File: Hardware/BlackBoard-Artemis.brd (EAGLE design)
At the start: 68.6 x 53.3 mm, 130 parts, among them IC3 LM1117, J2 CORTEX_DEBUG, J3 POWER_JACKTOE, J5 USB-C, Q1 1.1A/60V/600mΩ, U3 AP2112-3.3V, U4 ARTEMIS_MODULESMD, U5 CH340C, Y1 32.768kHz

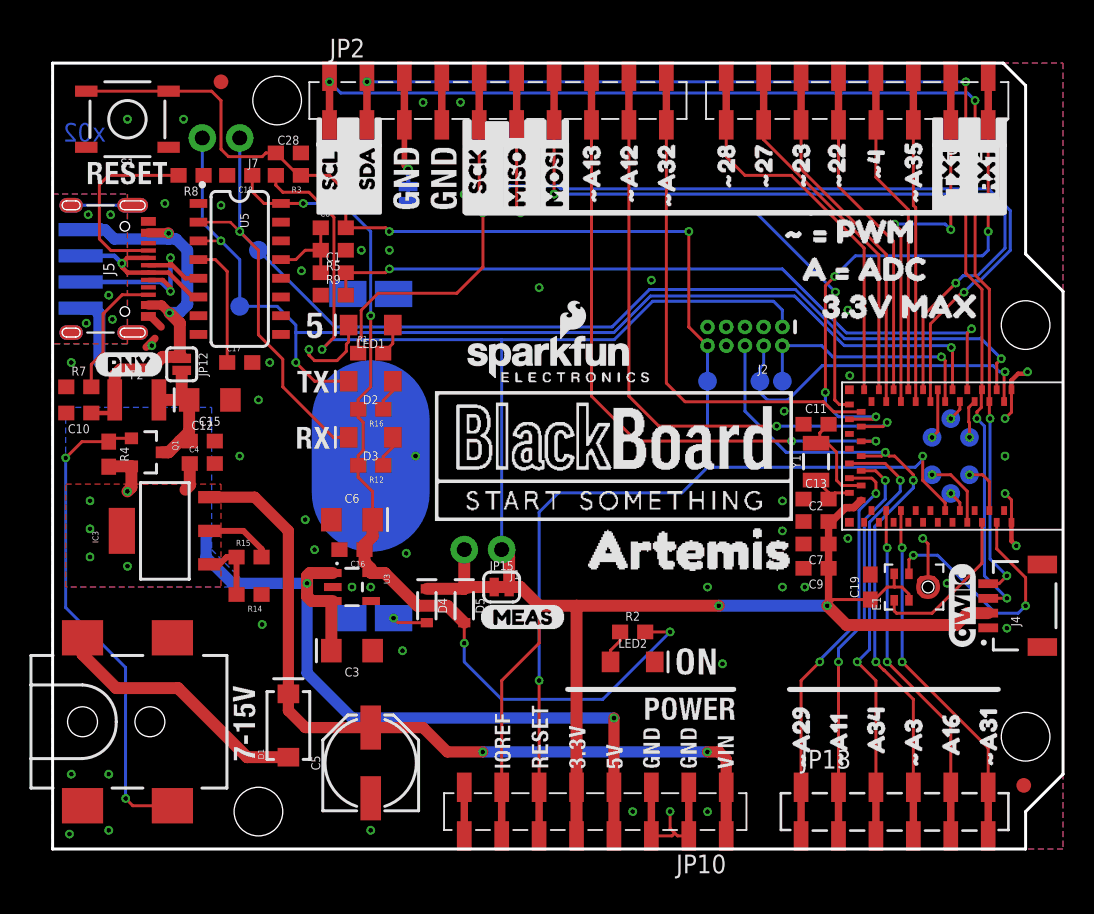
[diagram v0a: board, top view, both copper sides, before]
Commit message: Adding production panel
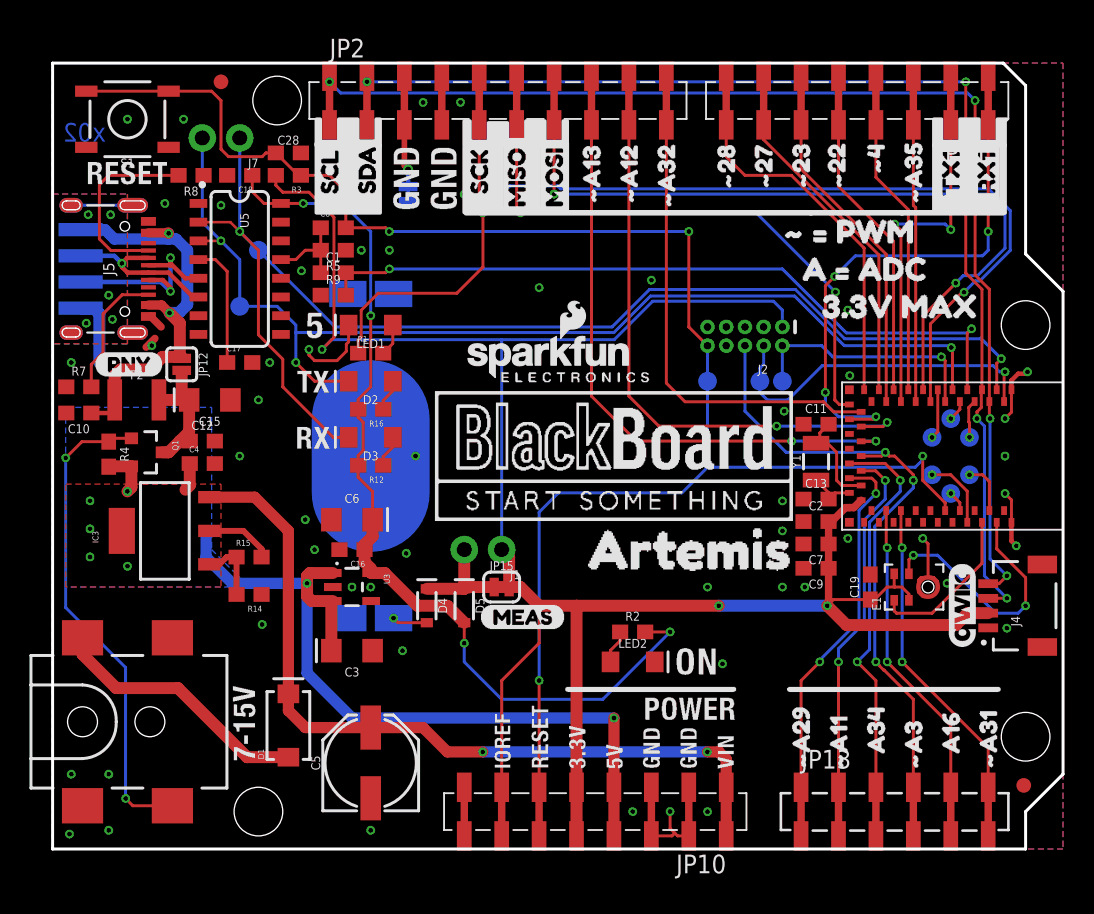
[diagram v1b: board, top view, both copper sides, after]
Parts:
- removed U$57: (no value), buzzard_labels (10):SCL3
- removed U$58: (no value), buzzard_labels (10):SDA4
- added U$18: (no value), buzzard_labels (6):SCL1
- added U$22: (no value), buzzard_labels (6):SDA0
- moved U$19 0.38 mm to (55.9, 44.8)
- moved U$17 0.13 mm to (61.0, 5.46)
- moved U$28 0.13 mm to (58.4, 4.45)
- moved U$29 0.13 mm to (53.3, 4.45)
- moved U$31 0.13 mm to (63.5, 4.45)
- moved U$50 0.13 mm to (29.0, 43.4)

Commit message: Fixing PWM on pin 7
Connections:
- net D7/MOSI renamed ~D7/MOSI
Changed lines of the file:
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@@
 <grid distance="0.05" unitdist="inch" unit="inch" style="lines" multiple="1" display="yes" altdistance="0.005" altunitdist="inch" altunit="inch"/>
 <layers>
-<layer number="1" name="Top" color="4" fill="1" visible="no" active="yes"/>
-<layer number="16" name="Bottom" color="1" fill="1" visible="no" active="yes"/>
+<layer number="1" name="Top" color="4" fill="1" visible="yes" active="yes"/>
+<layer number="16" name="Bottom" color="1" fill="1" visible="yes" active="yes"/>
 <layer number="17" name="Pads" color="2" fill="1" visible="yes" active="yes"/>
-<layer number="18" name="Vias" color="2" fill="1" visible="no" active="yes"/>
-<layer number="19" name="Unrouted" color="6" fill="1" visible="no" active="yes"/>
+<layer number="18" name="Vias" color="2" fill="1" visible="yes" active="yes"/>
+<layer number="19" name="Unrouted" color="6" fill="1" visible="yes" active="yes"/>
 <layer number="20" name="Dimension" color="24" fill="1" visible="yes" active="yes"/>
 <layer number="21" name="tPlace" color="16" fill="1" visible="yes" active="yes"/>
-<layer number="22" name="bPlace" color="14" fill="1" visible="no" active="yes"/>
+<layer number="22" name="bPlace" color="14" fill="1" visible="yes" active="yes"/>
 <layer number="23" name="tOrigins" color="15" fill="1" visible="yes" active="yes"/>
-<layer number="24" name="bOrigins" color="15" fill="1" visible="no" active="yes"/>
+<layer number="24" name="bOrigins" color="15" fill="1" visible="yes" active="yes"/>
 <layer number="25" name="tNames" color="7" fill="1" visible="no" active="yes"/>
 <layer number="26" name="bNames" color="7" fill="1" visible="no" active="yes"/>
-<layer number="27" name="tValues" color="7" fill="1" visible="yes" active="yes"/>
+<layer number="27" name="tValues" color="7" fill="1" visible="no" active="yes"/>
 <layer number="28" name="bValues" color="7" fill="1" visible="no" active="yes"/>
 <layer number="29" name="tStop" color="2" fill="3" visible="no" active="yes"/>
 <layer number="30" name="bStop" color="5" fill="6" visible="no" active="yes"/>
-<layer number="31" name="tCream" color="7" fill="4" visible="yes" active="yes"/>
+<layer number="31" name="tCream" color="7" fill="4" visible="no" active="yes"/>
 <layer number="32" name="bCream" color="7" fill="5" visible="no" active="yes"/>
 <layer number="33" name="tFinish" color="6" fill="3" visible="no" active="yes"/>
@@
 <wire x1="61.079" y1="33.9551" x2="61.079" y2="31.17" width="0.2032" layer="1"/>
 </signal>
-<signal name="D7/MOSI">
+<signal name="~D7/MOSI">
 <contactref element="JP2" pad="7B"/>
 <contactref element="JP2" pad="7A"/>

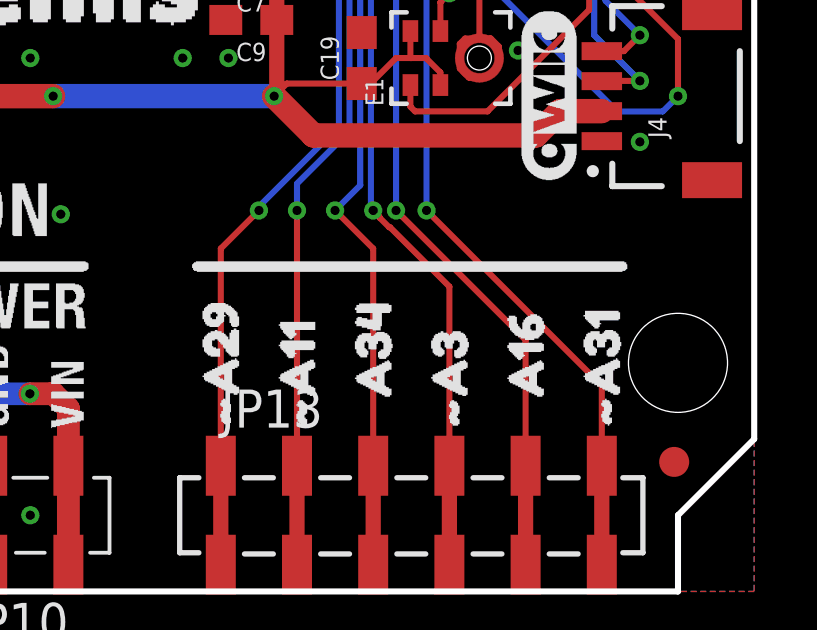
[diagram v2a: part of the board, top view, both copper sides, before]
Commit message: Fix pin 33 silk indicator error
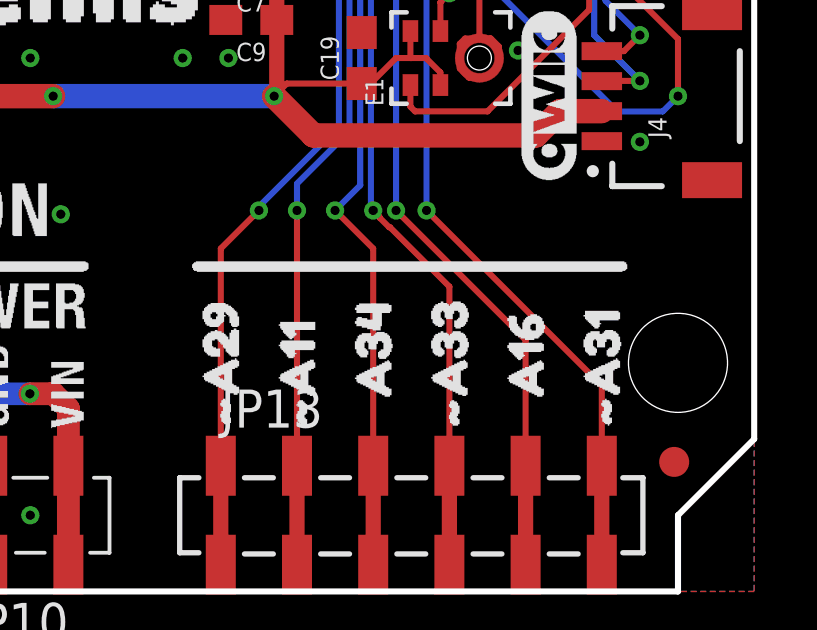
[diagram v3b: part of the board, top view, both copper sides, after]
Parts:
- removed U$28: (no value), buzzard_labels (1):#A31
- added U$37: (no value), buzzard_labels (6):#A332
- renumbered U4 to U1
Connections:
- net ~AD3/SWO renamed ~AD33/SWO

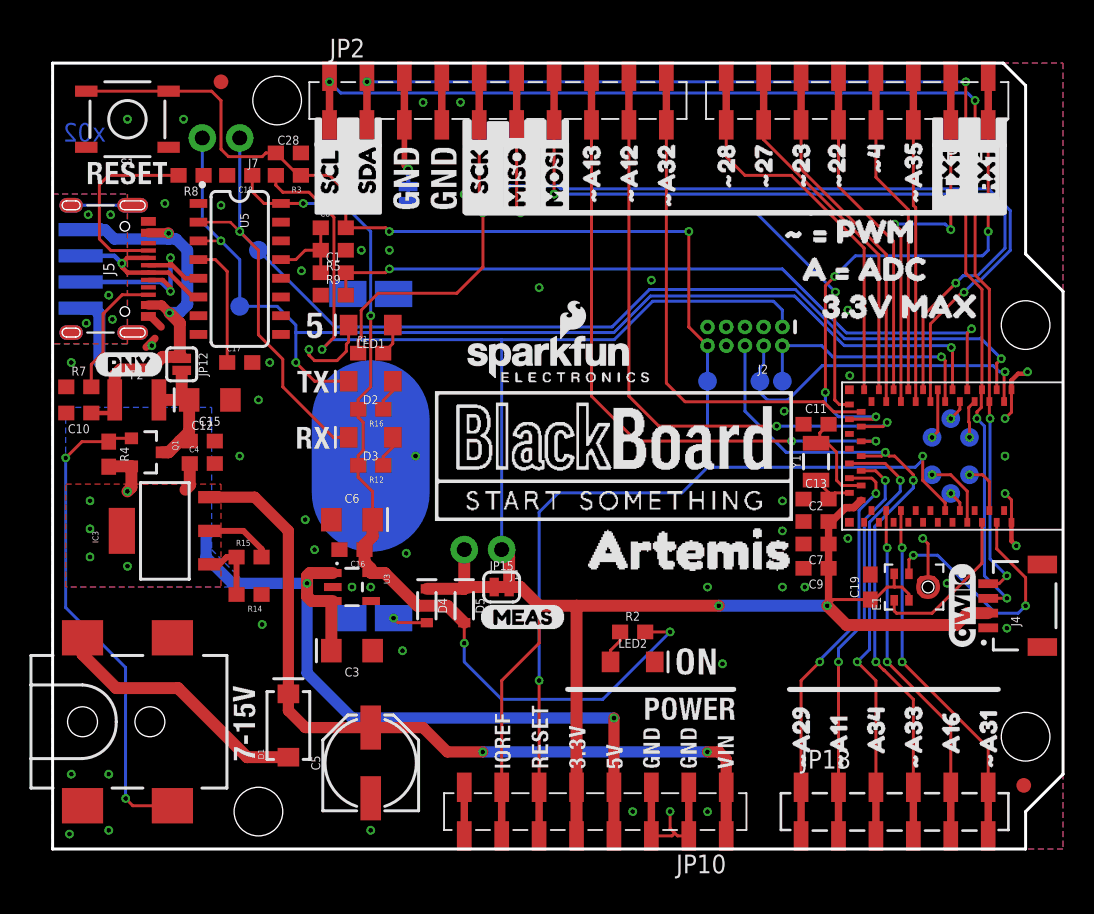
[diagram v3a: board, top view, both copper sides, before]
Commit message: Change labels to match variant.
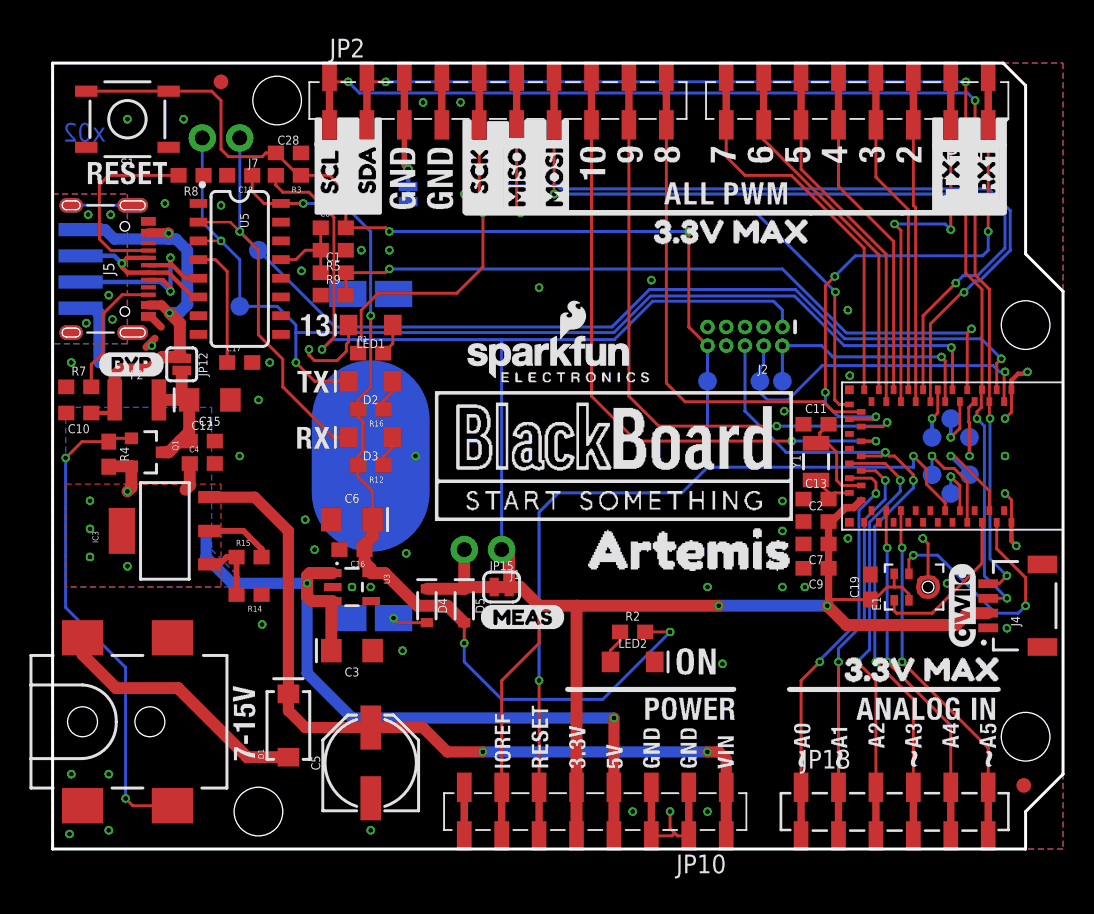
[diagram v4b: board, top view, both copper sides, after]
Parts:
- removed U$26: (no value), buzzard_labels (1):#2711
- removed U$27: (no value), buzzard_labels (1):#2812
- removed U$29: (no value), buzzard_labels (1):#A113
- removed U$30: (no value), buzzard_labels (1):#A294
- removed U$31: (no value), buzzard_labels (1):#A310
- removed U$33: (no value), buzzard_labels (1):#A357
- removed U$34: (no value), buzzard_labels (1):#A1214
- removed U$35: (no value), buzzard_labels (1):#A1315
- removed U$36: (no value), buzzard_labels (1):#A3213
- removed U$37: (no value), buzzard_labels (6):#A332
- removed U$38: (no value), buzzard_labels (1):A342
- removed U$60: (no value), buzzard_labels (1):#425
- removed U$61: (no value), buzzard_labels (1):#434
- removed U$62: (no value), buzzard_labels (1):80
- removed U$63: (no value), buzzard_labels (1):91
- removed U$64: (no value), buzzard_labels (1):102
- removed U$65: (no value), buzzard_labels (1):383
- removed U$66: (no value), buzzard_labels (2):#_#_PWM7
- removed U$69: (no value), buzzard_labels (2):A_#_ADC6
- added U$23: (no value), buzzard_labels (2):251
- added U$24: (no value), buzzard_labels (2):262
- added U$68: (no value), buzzard_labels (13):BYP0
- U$13: device buzzard_labels:PNY0 -> buzzard_labels (2):3#3V_MAX2
- U$17: device buzzard_labels:A160 -> buzzard_labels (2):#284
- U$19: device buzzard_labels (1):#48 -> buzzard_labels (2):#295
- U$21: device buzzard_labels (1):#229 -> buzzard_labels (2):240
- U$25: device buzzard_labels (1):#2310 -> buzzard_labels (2):273
- moved U$13 53.7 mm to (52.3, 12.2)
- moved U$25 24.2 mm to (66.5, 25.4), flipped to the bottom, turned to 0 degrees
- moved U$19 23.5 mm to (63.2, 22.5), flipped to the bottom, turned to 0 degrees
- moved U$17 20.1 mm to (58.8, 25.4), flipped to the bottom, turned to 0 degrees
- moved U$21 16.8 mm to (58.8, 27.9), flipped to the bottom, turned to 0 degrees
- moved U$67 12.5 mm to (39.4, 41.9)
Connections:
- net AD16 renamed D20/A4
- net AD34 renamed D18/A2
- net D10 renamed D26
- net D38 renamed D27
- net D40/SDA renamed D14/SDA
- net D8 renamed D24
- net D9 renamed D25
- net ~AD11 renamed ~D17/A1
- net ~AD12 renamed ~D9/A9
- net ~AD13 renamed ~D10/A10
- net ~AD29 renamed ~D16/A0
- net ~AD31 renamed ~D21/A5
- net ~AD32 renamed ~D8/A8
- net ~AD33/SWO renamed ~D19/A3
- net ~AD35 renamed ~D2/A6
- net ~D23 renamed ~D5
- net ~D24/TXO-1 renamed ~D1/TXO-1
- net ~D25/RXI-1 renamed ~D0/RXI-1
- net ~D27 renamed ~D6
- net ~D39/SCL renamed ~D15/SCL
- net ~D43 renamed ~D29
- net ~D5/SCK renamed ~D13/SCK
- net ~D6/MISO renamed ~D12/MISO
- net ~D7/MOSI renamed ~D11/MOSI
- removed net ~D22: JP11.5A, JP11.5B, U1.~D22
- removed net ~D42: TP9.P$1, U1.~D42
- new net ~D3: JP11.4A, JP11.4B, U1.~D4
- new net ~D7: JP11.8A, JP11.8B, U1.~D28
- net ~D28: now also TP9.P$1, U1.~D42; no longer JP11.8A, JP11.8B, U1.~D28
- net ~D4: now also JP11.5A, JP11.5B, U1.~D22; no longer JP11.4A, JP11.4B, U1.~D4
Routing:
- net ~D7: track 0.00 -> 27.0 mm
- net ~D22: track 22.8 -> 0.00 mm
- net ~D3: track 0.00 -> 22.2 mm
- net ~D28: track 27.0 -> 7.15 mm, vias 0 -> 1
- net ~D42: track 4.96 -> 0.00 mm, vias 1 -> 0
- net D27: track 3.51 -> 6.73 mm
- net D26: track 1.42 -> 3.96 mm
- net D25: track 2.62 -> 5.16 mm
- net ~D29: track 1.42 -> 3.70 mm
- net ~D4: track 22.2 -> 22.8 mm
